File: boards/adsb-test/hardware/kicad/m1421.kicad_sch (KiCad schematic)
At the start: 0 parts

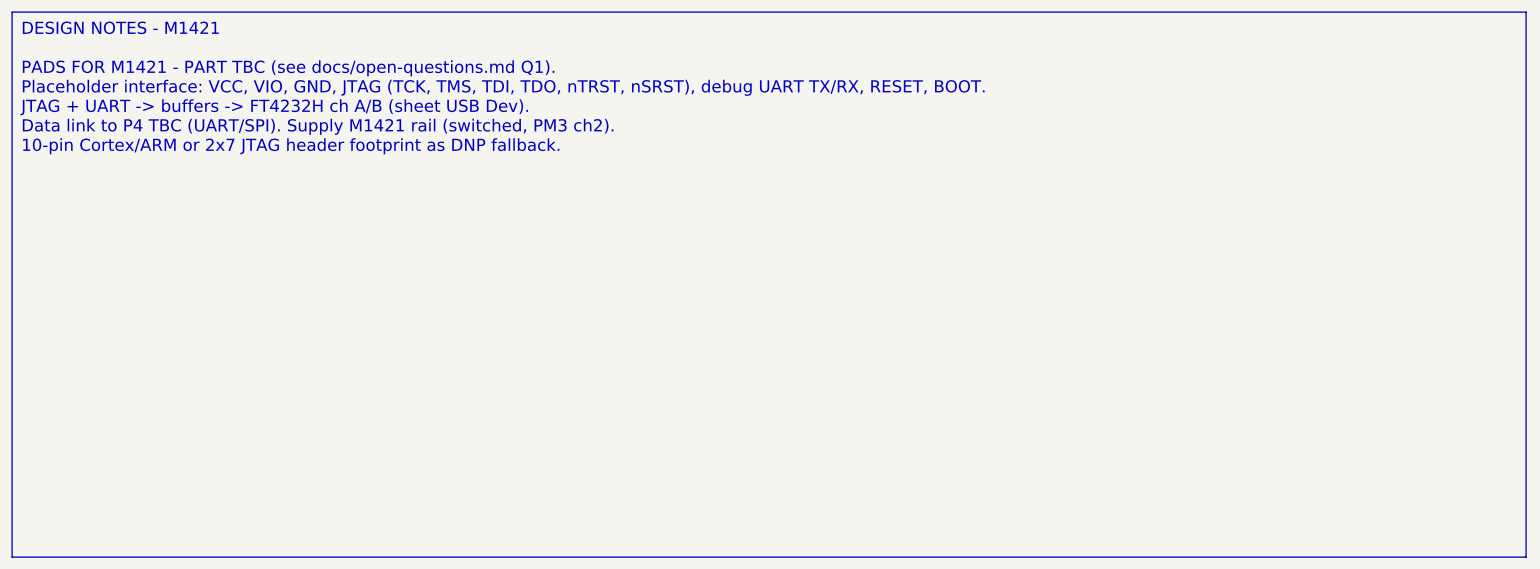
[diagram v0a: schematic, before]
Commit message: Release v0.4.0: ADSB_Test with ESP32-C5, ADSBee m1421 and LA5016 header
- C6 -> C5 co-processor; m1421 identified and integrated (symbol/footprint
  from the ADSBee 1421 carrier, GPL-3.0 attribution)
- Power budget and 2S1P battery sizing for >= 1 h; USB-A for 1-2 SDRs via hub
- Dev port: FT2232H + RP2040 debugprobe; TCA6408A expander for slow I/O
- Test Debug sheet with LA5016 header and rail test points
- Vendor documents git-ignored (public repo)

Co-Authored-By: Claude Opus 5.5 <noreply@anthropic.com>
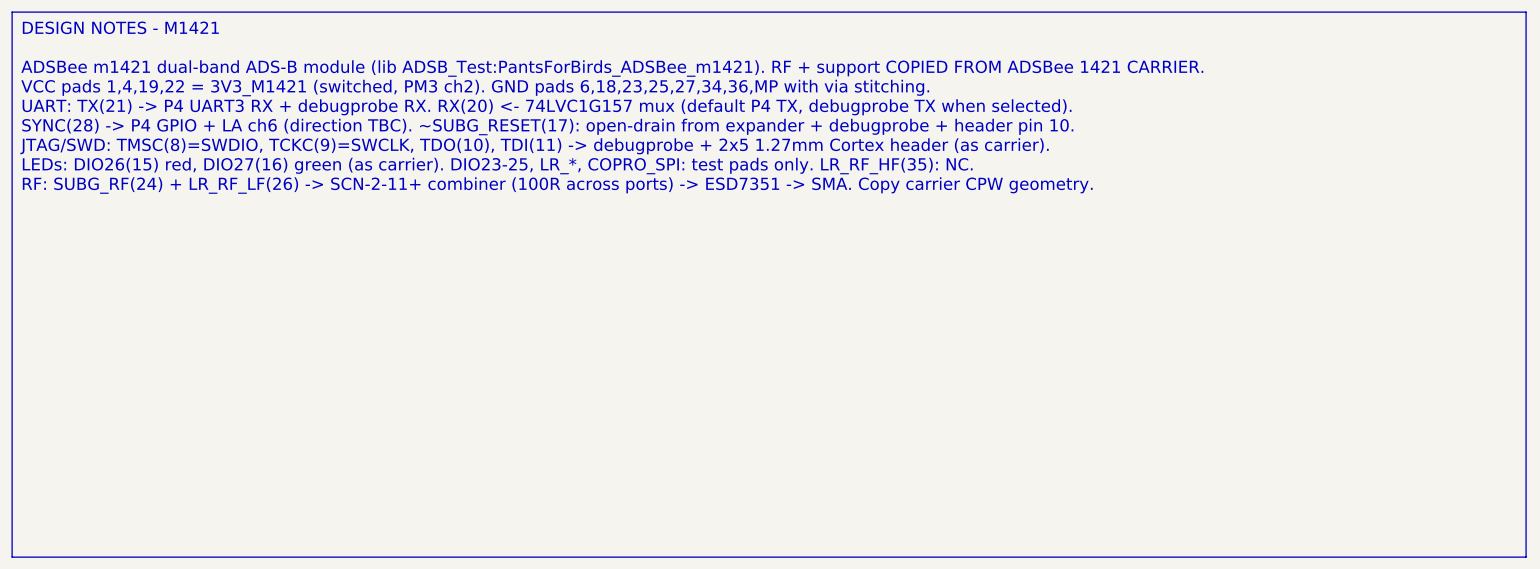
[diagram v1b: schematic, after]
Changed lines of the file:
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@@
 		(comment 1 "Requirements: boards/adsb-test/docs/requirements.md")
 	)
-	(text_box "DESIGN NOTES - M1421\n\nPADS FOR M1421 - PART TBC (see docs/open-questions.md Q1).\nPlaceholder interface: VCC, VIO, GND, JTAG (TCK, TMS, TDI, TDO, nTRST, nSRST), debug UART TX/RX, RESET, BOOT.\nJTAG + UART -> buffers -> FT4232H ch A/B (sheet USB Dev).\nData link to P4 TBC (UART/SPI). Supply M1421 rail (switched, PM3 ch2).\n10-pin Cortex/ARM or 2x7 JTAG header footprint as DNP fallback."
+	(text_box "DESIGN NOTES - M1421\n\nADSBee m1421 dual-band ADS-B module (lib ADSB_Test:PantsForBirds_ADSBee_m1421). RF + support COPIED FROM ADSBee 1421 CARRIER.\nVCC pads 1,4,19,22 = 3V3_M1421 (switched, PM3 ch2). GND pads 6,18,23,25,27,34,36,MP with via stitching.\nUART: TX(21) -> P4 UART3 RX + debugprobe RX. RX(20) <- 74LVC1G157 mux (default P4 TX, debugprobe TX when selected).\nSYNC(28) -> P4 GPIO + LA ch6 (direction TBC). ~SUBG_RESET(17): open-drain from expander + debugprobe + header pin 10.\nJTAG/SWD: TMSC(8)=SWDIO, TCKC(9)=SWCLK, TDO(10), TDI(11) -> debugprobe + 2x5 1.27mm Cortex header (as carrier).\nLEDs: DIO26(15) red, DIO27(16) green (as carrier). DIO23-25, LR_*, COPRO_SPI: test pads only. LR_RF_HF(35): NC.\nRF: SUBG_RF(24) + LR_RF_LF(26) -> SCN-2-11+ combiner (100R across ports) -> ESD7351 -> SMA. Copy carrier CPW geometry."
 		(exclude_from_sim no)
 		(at 20 20 0)
